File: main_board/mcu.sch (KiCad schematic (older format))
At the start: 8 parts

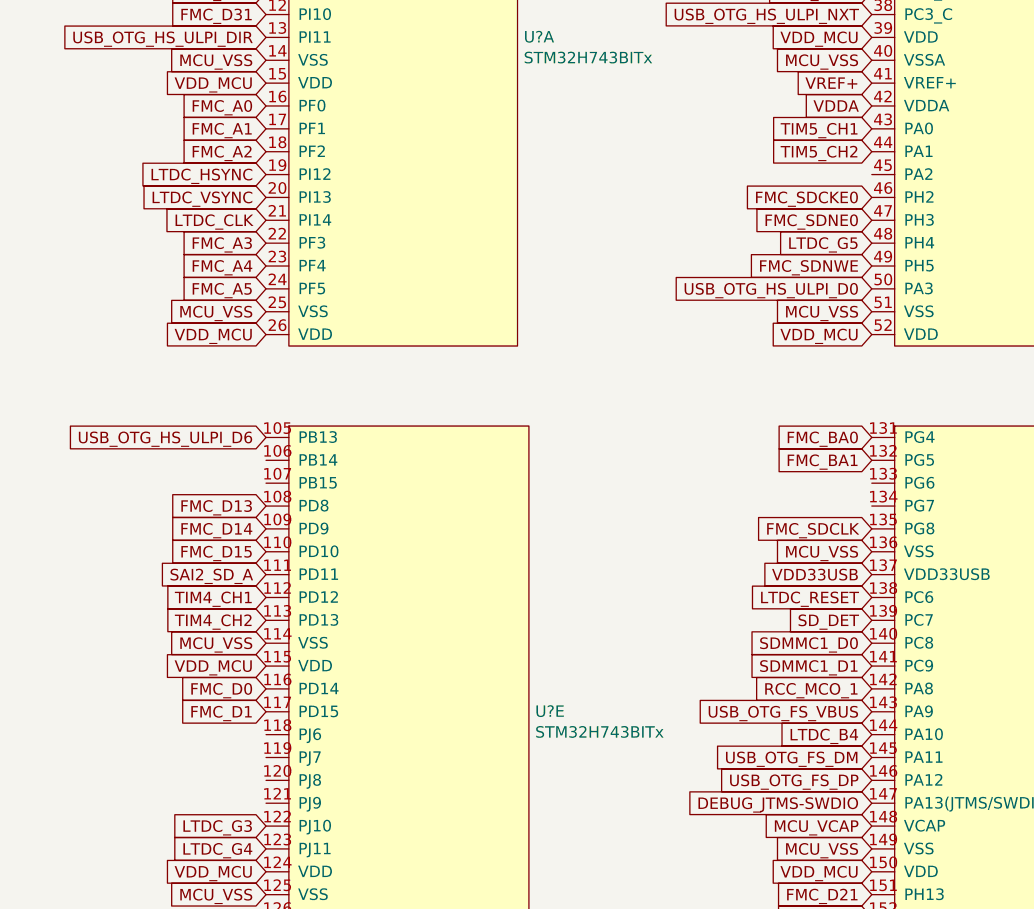
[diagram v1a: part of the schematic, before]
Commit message: Added MIDI connectors and SD card to io_board
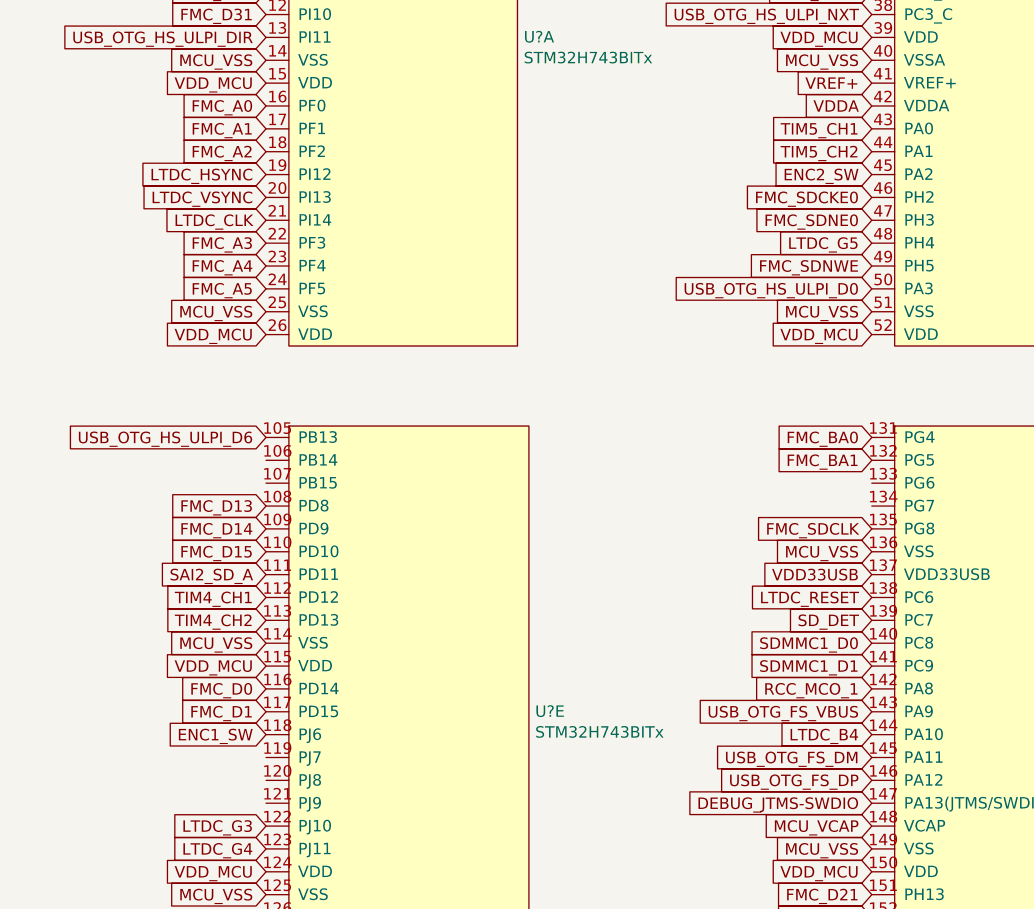
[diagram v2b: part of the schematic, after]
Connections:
- net ENC2_SW: now reaches U?.45 (PA2)
- net ENC1_SW: now reaches U?.118 (PJ6)
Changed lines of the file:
@@
 EESchema Schematic File Version 4
 LIBS:main_board-cache
-EELAYER 26 0
+EELAYER 29 0
 EELAYER END
 $Descr A4 11693 8268
 encoding utf-8
-Sheet 2 13
+Sheet 2 12
 Title ""
 Date ""
@@
 Text GLabel 4150 5250 0    50   Input ~ 0
 MCU_VCAP
+Text GLabel 4150 2400 0    50   Input ~ 0
+ENC2_SW
+Text GLabel 1500 4850 0    50   Input ~ 0
+ENC1_SW
 $EndSCHEMATC
